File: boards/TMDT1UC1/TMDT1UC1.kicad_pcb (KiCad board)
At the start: 4 copper layers, 51 parts, among them J1 TC2050, U1 DW3210, U2 STM32U575RGTx, U3 LIS2DH, U4 TPS61222DCK-FIXED, Y1 ABM8-38.400MHZ-12-D1G-T

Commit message: Started switching chips to simpler design on tag (needed factory calibration for reliable TWR)
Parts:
- removed AE1: Antenna_Chip 7000AT18A1600001E, RF_Antenna:Johanson_2450AT18x100
- removed BT1: CR2032-BS-6-1, meridian:BAT_CR2032-BS-6-1
- removed C1, C11, C16, C2, C20, C28, C29, C3, C4, C5: 100n, Capacitor_SMD:C_0402_1005Metric
- removed C10: 4u7, Capacitor_SMD:C_0603_1608Metric
- removed C12, C7: 10n, Capacitor_SMD:C_0402_1005Metric
- removed C13, C14, C6: 10u, Capacitor_SMD:C_0402_1005Metric
- removed C15: 100u, Capacitor_SMD:C_0603_1608Metric
- removed C17, C22, C23: 4n7, Capacitor_SMD:C_0402_1005Metric
- removed C18, C24, C25: 100n, Capacitor_SMD:C_0201_0603Metric
- removed C19: 220n, Capacitor_SMD:C_0201_0603Metric
- removed C21, C26: 10u, Capacitor_SMD:C_0603_1608Metric
- removed C27: 2p RF/DCBLOCK, Capacitor_SMD:C_0402_1005Metric
- removed C8, C9: 1u, Capacitor_SMD:C_0603_1608Metric
- removed FB1: 120R, Inductor_SMD:L_0603_1608Metric
- removed FB2: 33R, Inductor_SMD:L_0603_1608Metric
- removed H1, H2, H3, H4: MountingHole_Pad, MountingHole:MountingHole_3.2mm_M3_Pad_Via
- removed J1: TC2050, Connector:Tag-Connect_TC2050-IDC-NL_2x05_P1.27mm_Vertical
- removed L1: 4u7, Inductor_SMD:L_1210_3225Metric
- removed R1, R4: 10k, Resistor_SMD:R_0402_1005Metric
- removed R2: 100k, Resistor_SMD:R_0402_1005Metric
- removed R3: 50, Resistor_SMD:R_0402_1005Metric
- removed R5: 1k, Resistor_SMD:R_0402_1005Metric
- removed TP1, TP2: TestPoint, TestPoint:TestPoint_Pad_D1.0mm
- removed U1: DW3210, meridian:qfn_DW3210_QOR
- removed U2: STM32U575RGTx, Package_QFP:LQFP-64_10x10mm_P0.5mm
- removed U3: LIS2DH, Package_LGA:LGA-14_2x2mm_P0.35mm_LayoutBorder3x4y
- removed U4: TPS61222DCK-FIXED, Package_TO_SOT_SMD:Texas_R-PDSO-G6
- removed Y1: ABM8-38.400MHZ-12-D1G-T, meridian:XTAL_ABM8-38.400MHZ-12-D1G-T
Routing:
- net /DW_XTI: track 5.70 -> 0.00 mm
- net /DW_XTO: track 3.99 -> 0.00 mm
- net +3.3V: track 3.91 -> 0.00 mm
- net /DW_VTX_D: track 1.25 -> 0.00 mm

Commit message: Updated PCB (testing auto router)
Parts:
- added BT1: CR2032-BS-6-1, meridian:BAT_CR2032-BS-6-1, B.Cu at (90.0, 120.1)
- added C1: 100n, Capacitor_SMD:C_0402_1005Metric, F.Cu at (96.9, 119.8)
- added C10: 100n, Capacitor_SMD:C_0402_1005Metric, F.Cu at (80.1, 95.0)
- added C12: 10n, Capacitor_SMD:C_0402_1005Metric, B.Cu at (101.5, 107.0)
- added C13: 10u, Capacitor_SMD:C_0603_1608Metric, B.Cu at (101.2, 108.5)
- added C14: 10u, Capacitor_SMD:C_0603_1608Metric, B.Cu at (99.0, 101.2)
- added C15: 100u, Capacitor_SMD:C_0603_1608Metric, B.Cu at (97.2, 101.2)
- added C16: 100n, Capacitor_SMD:C_0402_1005Metric, B.Cu at (100.5, 101.5)
- added C2: 100n, Capacitor_SMD:C_0402_1005Metric, F.Cu at (104.9, 117.9)
- added C28: 100n, Capacitor_SMD:C_0402_1005Metric, F.Cu at (82.6, 109.1)
- added C29: 100n, Capacitor_SMD:C_0402_1005Metric, F.Cu at (82.6, 113.1)
- added C3: 100n, Capacitor_SMD:C_0402_1005Metric, F.Cu at (96.9, 122.8)
- added C4: 100n, Capacitor_SMD:C_0402_1005Metric, F.Cu at (87.2, 113.1)
- added C5: 100n, Capacitor_SMD:C_0402_1005Metric, F.Cu at (92.8, 126.9)
- added C6: 10u, Capacitor_SMD:C_0603_1608Metric, F.Cu at (97.2, 121.4)
- added C7: 10u, Capacitor_SMD:C_0603_1608Metric, F.Cu at (79.8, 97.8)
- added C8: 100n, Capacitor_SMD:C_0402_1005Metric, F.Cu at (80.1, 100.6)
- added C9: 47u, Capacitor_SMD:C_0603_1608Metric, F.Cu at (79.8, 99.3)
- added DWM1: DWM3000, RF_Module:DWM1000, F.Cu at (90.0, 93.0)
- added H1: MountingHole_Pad, MountingHole:MountingHole_3.2mm_M3_Pad_Via, F.Cu at (74.0, 84.0)
- added H2: MountingHole_Pad, MountingHole:MountingHole_3.2mm_M3_Pad_Via, F.Cu at (106.0, 84.0)
- added H3: MountingHole_Pad, MountingHole:MountingHole_3.2mm_M3_Pad_Via, F.Cu at (106.0, 136.0)
- added H4: MountingHole_Pad, MountingHole:MountingHole_3.2mm_M3_Pad_Via, F.Cu at (74.0, 136.0)
- added J1: TC2050, Connector:Tag-Connect_TC2050-IDC-NL_2x05_P1.27mm_Vertical, F.Cu at (90.0, 135.1)
- added L1: 4u7, Inductor_SMD:L_1210_3225Metric, B.Cu at (104.8, 104.5)
- added R1: 10k, Resistor_SMD:R_0402_1005Metric, F.Cu at (90.8, 127.0)
- added R2: 100k, Resistor_SMD:R_0402_1005Metric, B.Cu at (101.9, 101.5)
- added R3: 10k, Resistor_SMD:R_0402_1005Metric, F.Cu at (102.3, 105.1)
- added R4: 100k, Resistor_SMD:R_0402_1005Metric, F.Cu at (99.9, 95.0)
- added R5: 1k, Resistor_SMD:R_0402_1005Metric, F.Cu at (88.8, 131.1)
- added R6: 10k, Resistor_SMD:R_0402_1005Metric, F.Cu at (80.1, 93.6)
- added U1: STM32U073CBTx, Package_QFP:LQFP-48_7x7mm_P0.5mm, F.Cu at (90.0, 120.0)
- added U2: W25Q128JVS, Package_SO:SOIC-8_5.3x5.3mm_P1.27mm, F.Cu at (103.0, 111.5)
- added U4: TPS61222DCK-FIXED, Package_TO_SOT_SMD:Texas_R-PDSO-G6, B.Cu at (101.2, 104.5)
- added U5: ADXL343, Package_LGA:LGA-14_3x5mm_P0.8mm_LayoutBorder1x6y, F.Cu at (79.5, 111.1)
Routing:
- net +3.3V: track 0.00 -> 131.6 mm, vias 0 -> 2
- net GND: track 0.00 -> 57.2 mm, vias 0 -> 24
- net /UWB_MOSI: track 0.00 -> 33.5 mm, vias 0 -> 2
- net /UWB_MISO: track 0.00 -> 32.6 mm, vias 0 -> 2
- net /UWB_CS: track 0.00 -> 30.3 mm, vias 0 -> 2
- net /PWR_BAT: track 0.00 -> 28.8 mm
- net /UWB_SCK: track 0.00 -> 26.7 mm, vias 0 -> 2
- net /IMU_MISO: track 0.00 -> 23.8 mm, vias 0 -> 2
- net /NRST: track 0.00 -> 23.5 mm
- net /SWDIO: track 0.00 -> 22.2 mm, vias 0 -> 2
- net /FLASH_MISO: track 0.00 -> 21.4 mm, vias 0 -> 2
- net /IMU_MOSI: track 0.00 -> 19.3 mm
- net /FLASH_CS: track 0.00 -> 19.3 mm
- net /SWDCLK: track 0.00 -> 17.4 mm, vias 0 -> 2
- net /IMU_SCK: track 0.00 -> 17.3 mm
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- added copper zone on B.Cu, net GND
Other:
- board outline added: 40 x 60 mm
- copper layers 4 -> 2

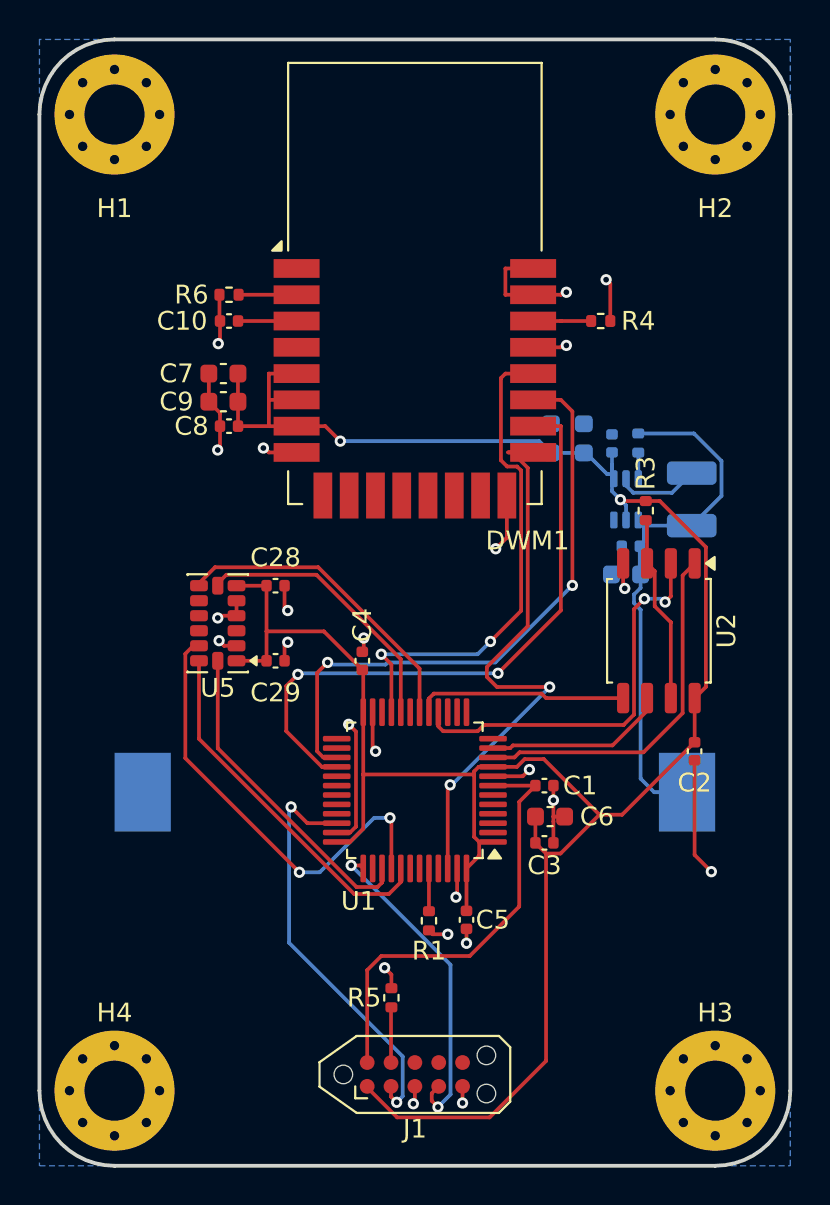
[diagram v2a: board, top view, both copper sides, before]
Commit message: Updated board (switched to 4 layer, rerouted cleaner)
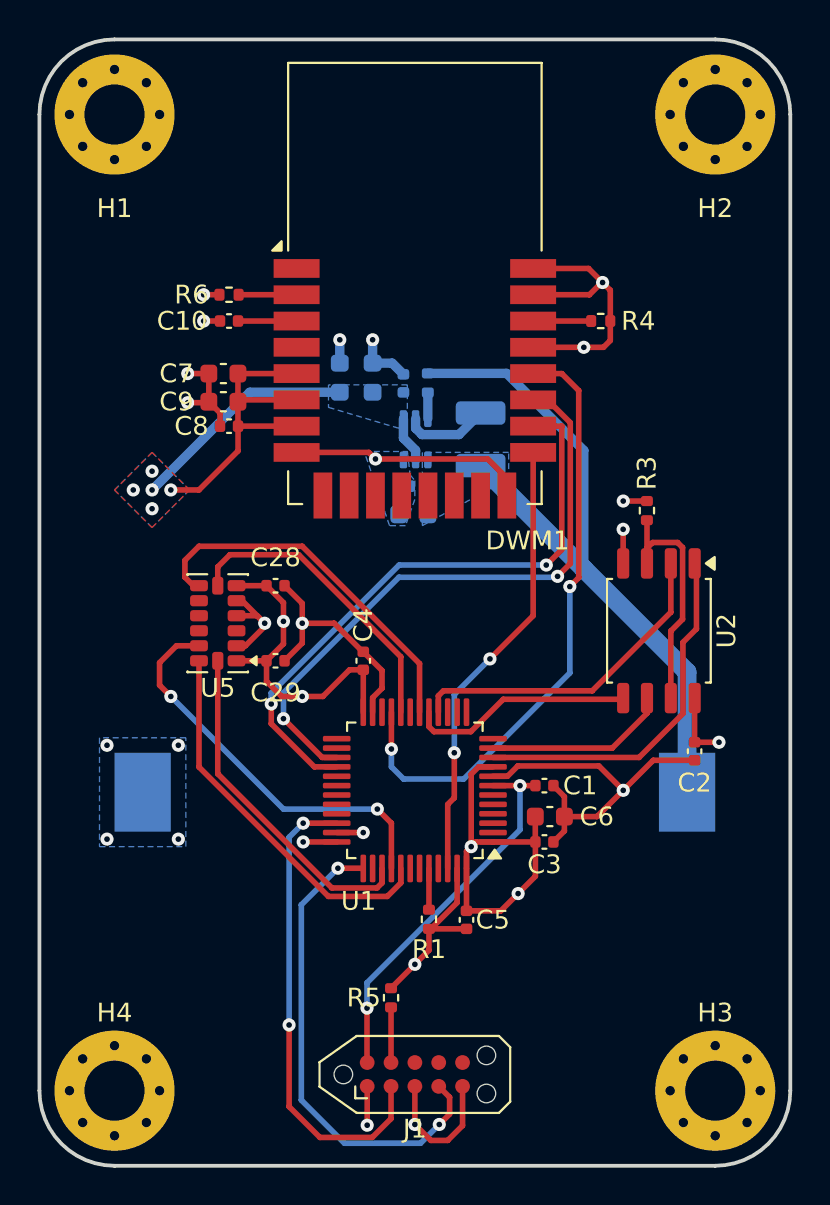
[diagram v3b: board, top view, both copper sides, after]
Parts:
- moved C13 11.8 mm to (89.9, 105.3)
- moved C12 11.7 mm to (90.2, 103.8)
- moved C14 11.7 mm to (87.8, 98.0)
- moved C15 11.7 mm to (86.0, 98.0)
- moved L1 11.7 mm to (93.5, 101.3)
- moved R2 11.7 mm to (90.7, 98.3)
- moved U4 11.7 mm to (90.0, 101.3)
- moved C16 11.6 mm to (89.4, 98.3)
- moved R1 0.08 mm to (90.8, 126.9)
- moved R3 0.06 mm to (102.4, 105.1)
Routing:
- net +3.3V: track 131.6 -> 78.6 mm, vias 2 -> 13
- net GND: track 57.2 -> 97.8 mm, vias 24 -> 20
- net /PWR_BAT: track 28.8 -> 38.3 mm
- net /SWDCLK: track 17.4 -> 25.9 mm
- net /UWB_SCK: track 26.7 -> 33.1 mm
- net /UWB_CS: track 30.3 -> 24.0 mm
- net /FLASH_MISO: track 21.4 -> 17.7 mm, vias 2 -> 0
- net Net-(U2-~{HOLD}/~{RESET}/IO_{3}): track 10.0 -> 13.5 mm
- net /SWDIO: track 22.2 -> 25.4 mm
- net /NRST: track 23.5 -> 20.4 mm, vias 0 -> 2
- net /IMU_INT: track 16.8 -> 19.8 mm
- net /IMU_MISO: track 23.8 -> 21.5 mm
- net /IMU_CS: track 14.8 -> 16.2 mm
- net /IMU_MOSI: track 19.3 -> 20.3 mm
- net /IMU_SCK: track 17.3 -> 18.2 mm
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- added copper zone on B.Cu, net +3.3V
- added copper zone on F.Cu, net +3.3V
- added copper zone on In1.Cu, net +3.3V
- added copper zone on B.Cu, net /PWR_BAT
- added copper zone on In2.Cu, net GND
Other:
- copper layers 2 -> 4
